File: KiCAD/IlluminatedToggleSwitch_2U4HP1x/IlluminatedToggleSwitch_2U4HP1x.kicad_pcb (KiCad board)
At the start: 2 copper layers, 20.3 x 84.1 mm, 4 parts, among them J1 Conn_01x03_Socket, SW1 SW_SPST_MOUNT

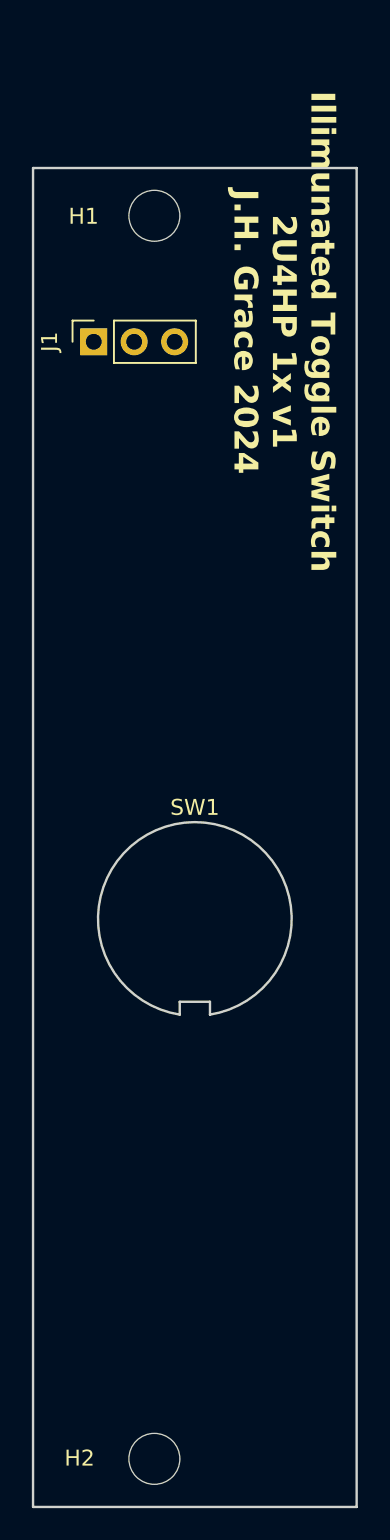
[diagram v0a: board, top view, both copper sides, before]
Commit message: updated PCB widths to better conform to Eurorack standards
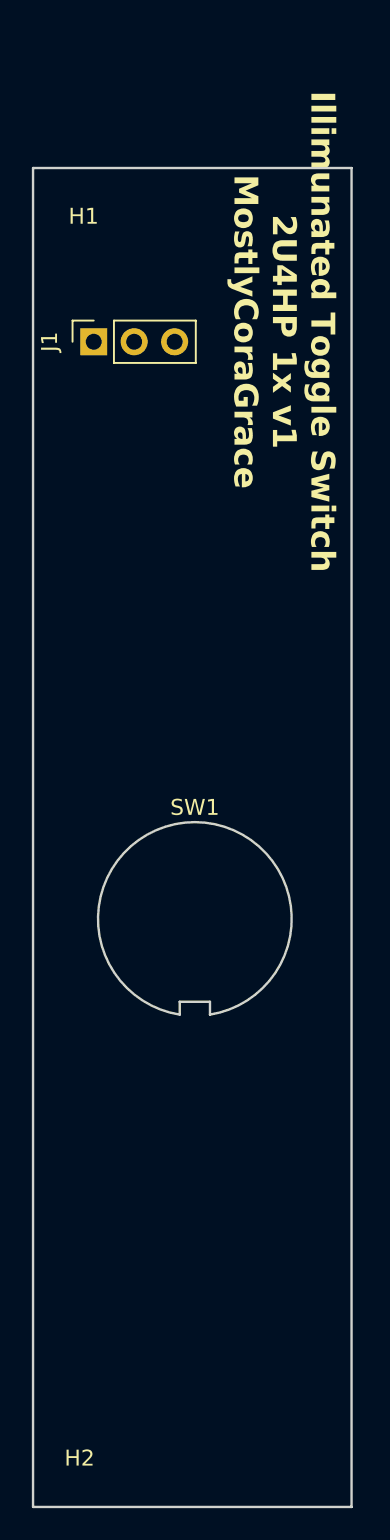
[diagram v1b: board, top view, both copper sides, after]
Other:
- board size 20.3 x 84.1 mm -> 20 x 84.1 mm
- board text added: "Illimunated Toggle Switch 2U4HP 1x v1 MostlyCoraGrace"
- board text removed: "Illimunated Toggle Switch 2U4HP 1x v1 J.H. Grace 2024"

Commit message: removed all front silkscreen, and flipped most modules, to make the boards 'cleaner'.
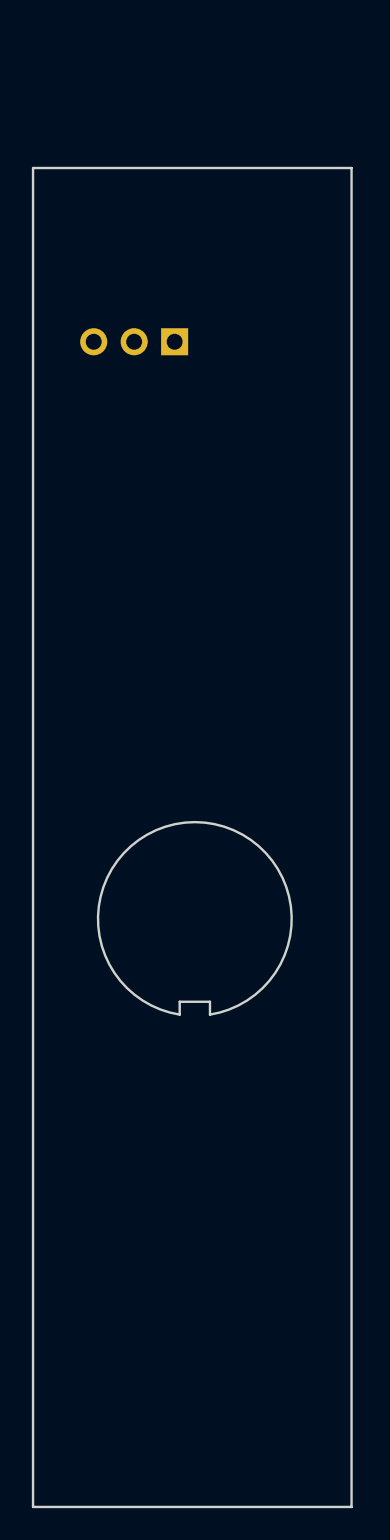
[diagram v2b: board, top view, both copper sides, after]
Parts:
- H1, H2, J1, SW1: moved to B.Cu
- moved J1 5.08 mm to (8.89, 13.3)
- turned H1 to 180 degrees
- turned H2 to 180 degrees
- turned SW1 to 180 degrees

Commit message: added copper fills to every module, to maybe possibly increase structural rigidity.
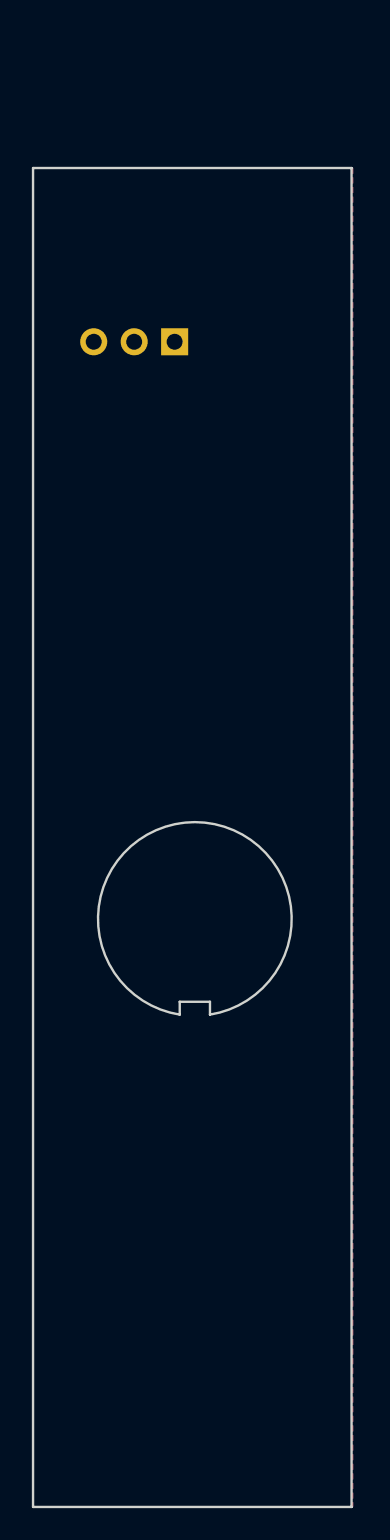
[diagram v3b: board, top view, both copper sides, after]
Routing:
- added copper zone on B.Cu, net (none)
- added copper zone on F.Cu, net (none)
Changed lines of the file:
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@@
+		)
+	)
+	(zone
+		(net 0)
+		(net_name "")
+		(layers "F&B.Cu")
+		(hatch edge 0.5)
+		(connect_pads
+			(clearance 0.5)
+		)
+		(min_thickness 0.25)
+		(filled_areas_thickness no)
+		(fill yes
+			(thermal_gap 0.5)
+			(thermal_bridge_width 0.5)
+			(island_removal_mode 1)
+			(island_area_min 10)
+		)
+		(polygon
+			(pts
+				(xy 0 2.413) (xy 20.066 2.413) (xy 20.066 86.487) (xy 0 86.487)
+			)
 		)
 	)

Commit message: added PCBWay print identification silkscreen text to each component
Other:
- board text added: "WayWayWay"
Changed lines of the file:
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@@
+		)
+	)
+	(gr_text "WayWayWay"
+		(at 1.25 16 90)
+		(layer "B.SilkS")
+		(effects
+			(font
+				(size 1 1)
+				(thickness 0.15)
+			)
+			(justify left top mirror)
 		)
 	)
